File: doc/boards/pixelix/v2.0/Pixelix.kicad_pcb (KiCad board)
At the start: 2 copper layers, 101 x 50 mm, 32 parts, among them J1 Conn_01x02, J2 Conn_01x02, J3 Conn_01x03, J4 Conn_01x02, J5 Conn_02x05_Odd_Even, J6 Conn_01x02, J7 Conn_01x03, J8 Conn_01x02, Q1 NMOS_GSD_BSS138, Q2 PMOS_GDS_STD26P3LLH6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

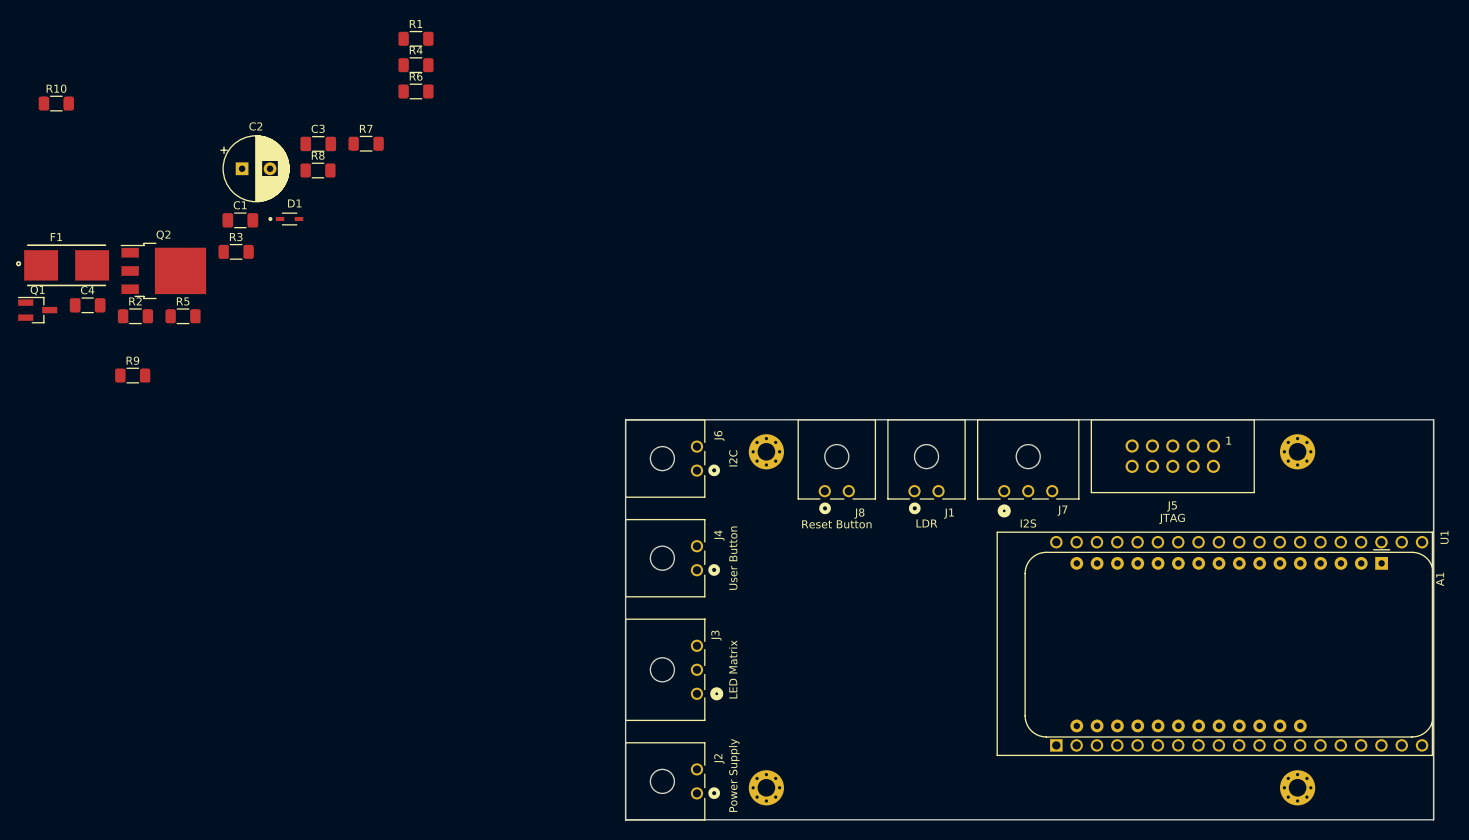
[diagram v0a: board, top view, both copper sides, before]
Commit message: Board v2.0 PCB - placed other components (R,C,FETs,...) - start routing
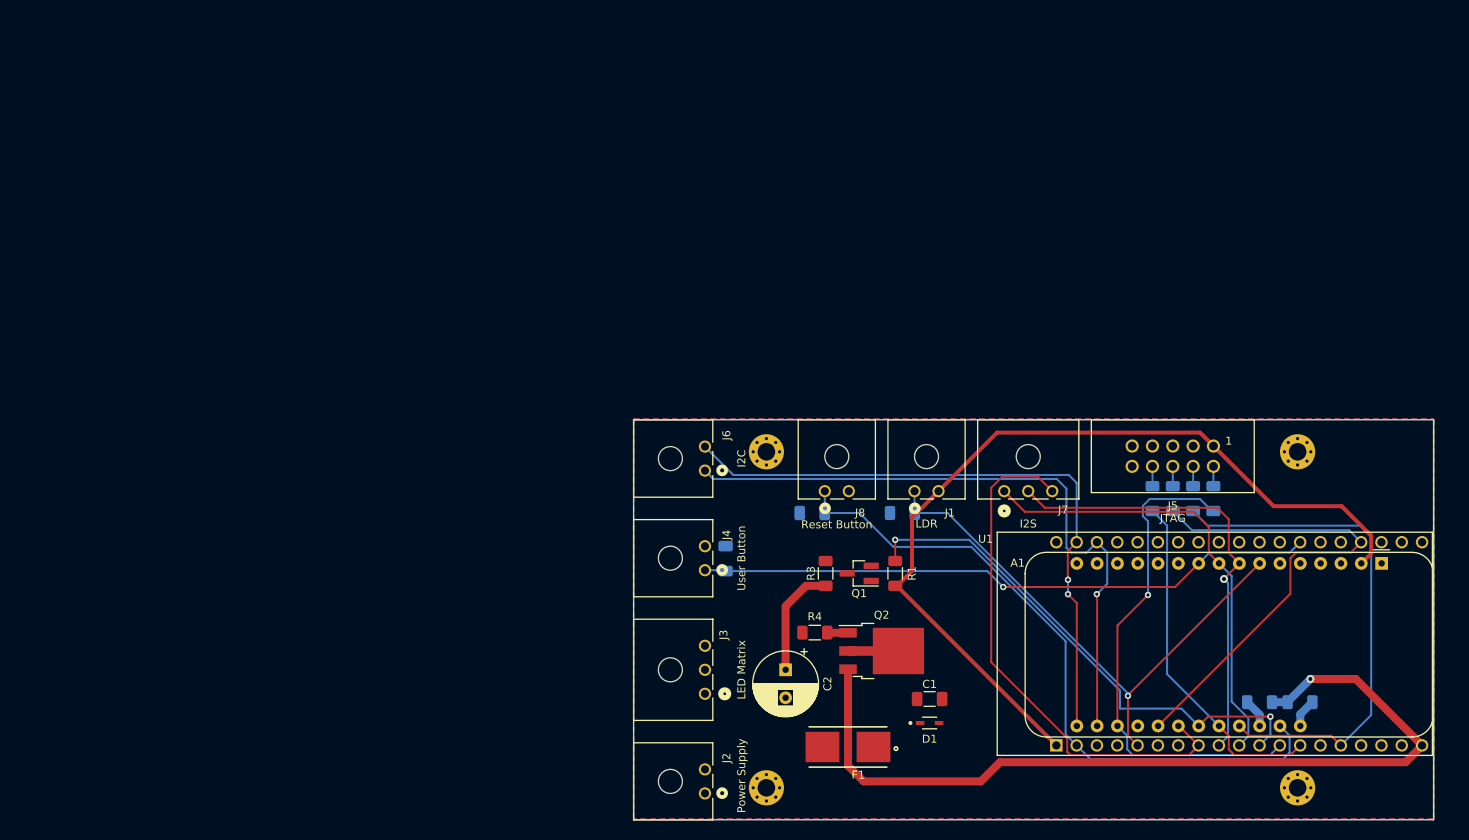
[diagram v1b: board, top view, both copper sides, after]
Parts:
- C3, C4, R10, R2, R5, R6, R7, R8, R9: moved to B.Cu
- moved R10 168.0 mm to (179.2, 105.4)
- moved R9 151.5 mm to (184.3, 105.4), turned to 180 degrees
- moved R5 130.8 mm to (173.5, 80.0), turned to -90 degrees
- moved F1 114.7 mm to (127.8, 111.0), turned to 180 degrees
- moved R8 112.1 mm to (165.9, 80.0), turned to -90 degrees
- moved R7 110.2 mm to (168.4, 80.0), turned to -90 degrees
- moved R6 109.7 mm to (170.9, 80.0), turned to -90 degrees
- moved Q1 107.8 mm to (129.2, 89.3), turned to 180 degrees
- moved C1 104.9 mm to (138.0, 105.0)
- moved D1 101.8 mm to (138.0, 108.0)
- moved Q2 101.5 mm to (132.0, 99.0)
- moved R2 99.0 mm to (134.6, 81.8), turned to 180 degrees
- moved C4 94.2 mm to (123.3, 81.8), turned to 180 degrees
- moved C2 92.4 mm to (120.0, 101.3), turned to -90 degrees
- moved R1 89.7 mm to (133.7, 89.3), turned to 90 degrees
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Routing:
- net /VCC-PROTECTED: track 0.00 -> 123.8 mm, vias 0 -> 1
- net +3V3: track 0.00 -> 109.7 mm
- net /RESET: track 0.00 -> 84.6 mm
- net /SCL: track 0.00 -> 82.2 mm, vias 0 -> 1
- net /SDA: track 0.00 -> 79.6 mm, vias 0 -> 2
- net /USER-BUTTON: track 0.00 -> 77.6 mm, vias 0 -> 1
- net /LDR-ANALOG-IN: track 0.00 -> 69.2 mm, vias 0 -> 1
- net /I2S_Data_IN: track 0.00 -> 66.5 mm
- net /LV-DATA-OUT: track 0.00 -> 65.2 mm, vias 0 -> 2
- net /MTCK: track 0.00 -> 65.0 mm
- net /MTDO: track 0.00 -> 62.6 mm
- net /MTMS: track 0.00 -> 62.4 mm, vias 0 -> 1
- net /I2S_CLK: track 0.00 -> 57.2 mm
- net /I2S_WS: track 0.00 -> 56.8 mm, vias 0 -> 1
- net /MTDI: track 0.00 -> 43.5 mm
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- added copper zone on B.Cu, net GND
- added copper zone on F.Cu, net GND
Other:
- board size 101 x 50 mm -> 100 x 50 mm

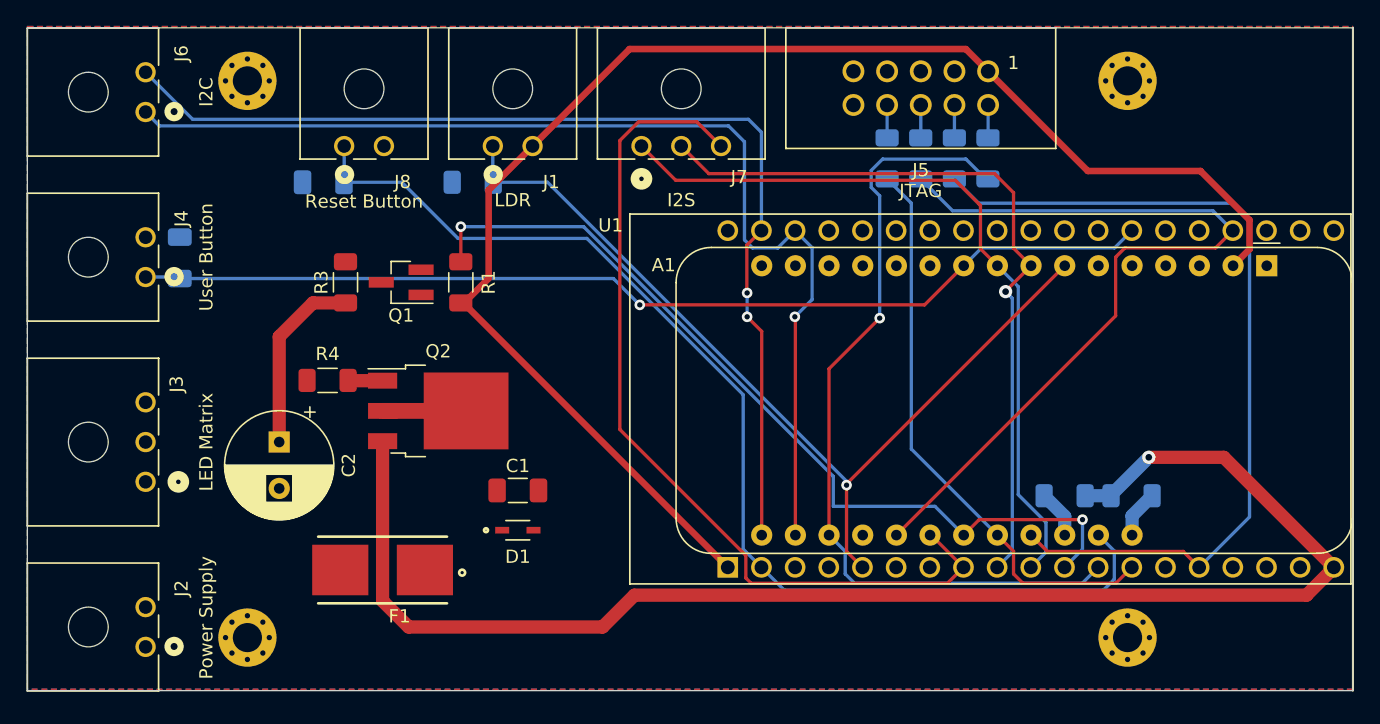
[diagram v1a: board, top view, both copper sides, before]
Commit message: Board v2.0 PCB - routing finished
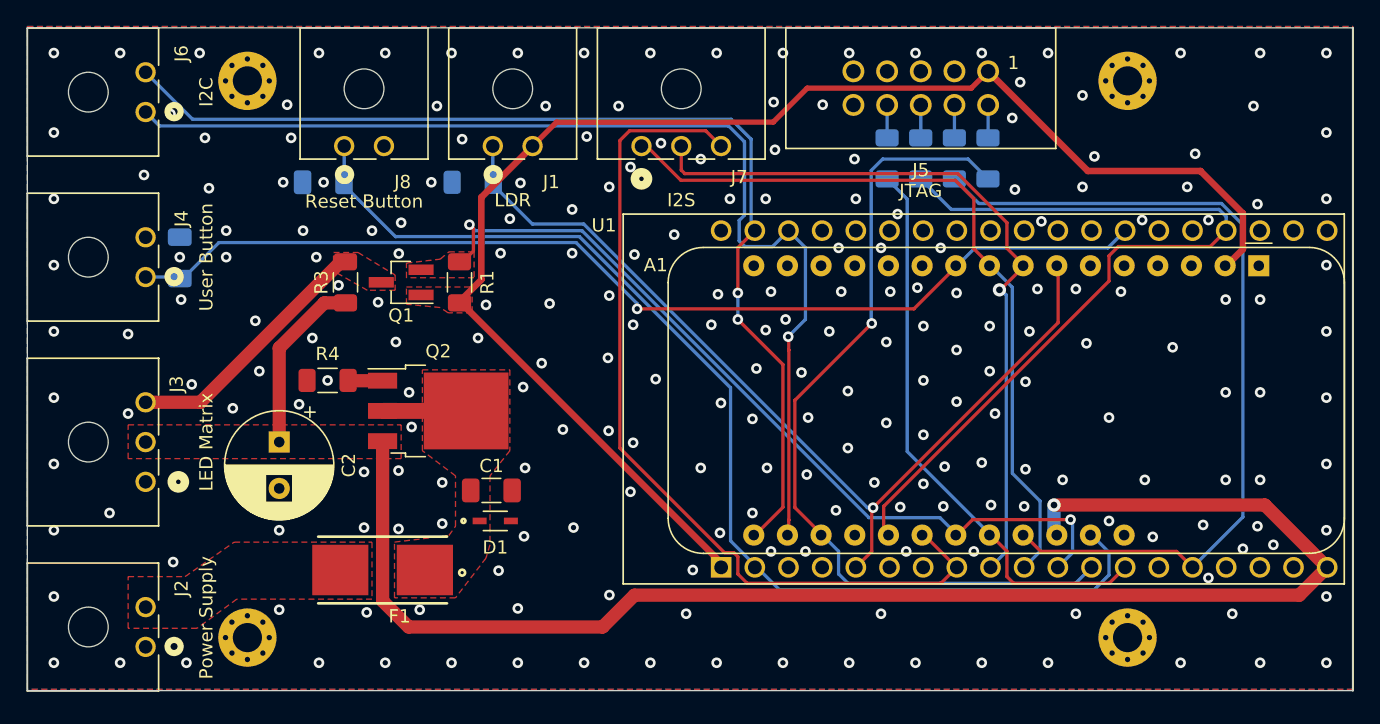
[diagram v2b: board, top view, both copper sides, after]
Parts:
- removed R10, R9: 0, Resistor_SMD:R_1206_3216Metric_Pad1.30x1.75mm_HandSolder
- moved C1 1.99 mm to (136.0, 105.0)
- moved D1 1.84 mm to (136.3, 107.3)
- moved A1 0.60 mm to (193.9, 88.0)
- moved U1 0.50 mm to (173.1, 98.1)
- moved R1 0.10 mm to (133.6, 89.3)
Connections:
- A1 pad 26: Net-(A1-Pad26) -> /VCC-PROTECTED
- A1 pad 28: Net-(A1-Pad28) -> unconnected-(A1-Pad28)
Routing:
- net /HV-DATA-OUT: track 0.00 -> 19.5 mm
- net Net-(A1-Pad26): track 3.61 -> 0.00 mm
- net Net-(A1-Pad28): track 3.59 -> 0.00 mm
- net +3V3: track 109.7 -> 107.0 mm
- net /USER-BUTTON: track 77.6 -> 79.8 mm
- net /LV-DATA-OUT: track 65.2 -> 63.1 mm
- net /LDR-ANALOG-IN: track 69.2 -> 70.8 mm
- net /MTMS: track 62.4 -> 63.9 mm
- net /SDA: track 79.6 -> 80.6 mm
- net /MTCK: track 65.0 -> 64.3 mm
- net /I2S_WS: track 56.8 -> 56.2 mm
- net /VCC-PROTECTED: track 123.8 -> 124.5 mm
- net /MTDO: track 62.6 -> 63.2 mm
- net GND: vias 0 -> 229
- added copper zone on F.Cu, net +3V3
- added copper zone on F.Cu, net /HV-DATA-OUT
- added copper zone on F.Cu, net /LV-DATA-OUT
- added copper zone on F.Cu, net /VCC-PROTECTED
- added copper zone on F.Cu, net Net-(C1-Pad1)
- added copper zone on F.Cu, net Net-(F1-Pad2)

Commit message: Board v2.0 PCB - small changes - create step file
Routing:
- net /MTMS: track 63.9 -> 65.2 mm
- net /RESET: track 84.1 -> 84.7 mm
- net GND: vias 229 -> 232

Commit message: Board v2.0 PCB - labeling PCB
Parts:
- added G***: LOGO, footprints:Pixelix_Logo_footprint, F.Cu at (186.3, 81.6)
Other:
- board text added: "${REVISION}"
- board text added: "BOT"
- board text added: "BlueAndi/esp-rgb-led-matrix"
- board text added: "Github Repository:"
- board text added: "TOP"

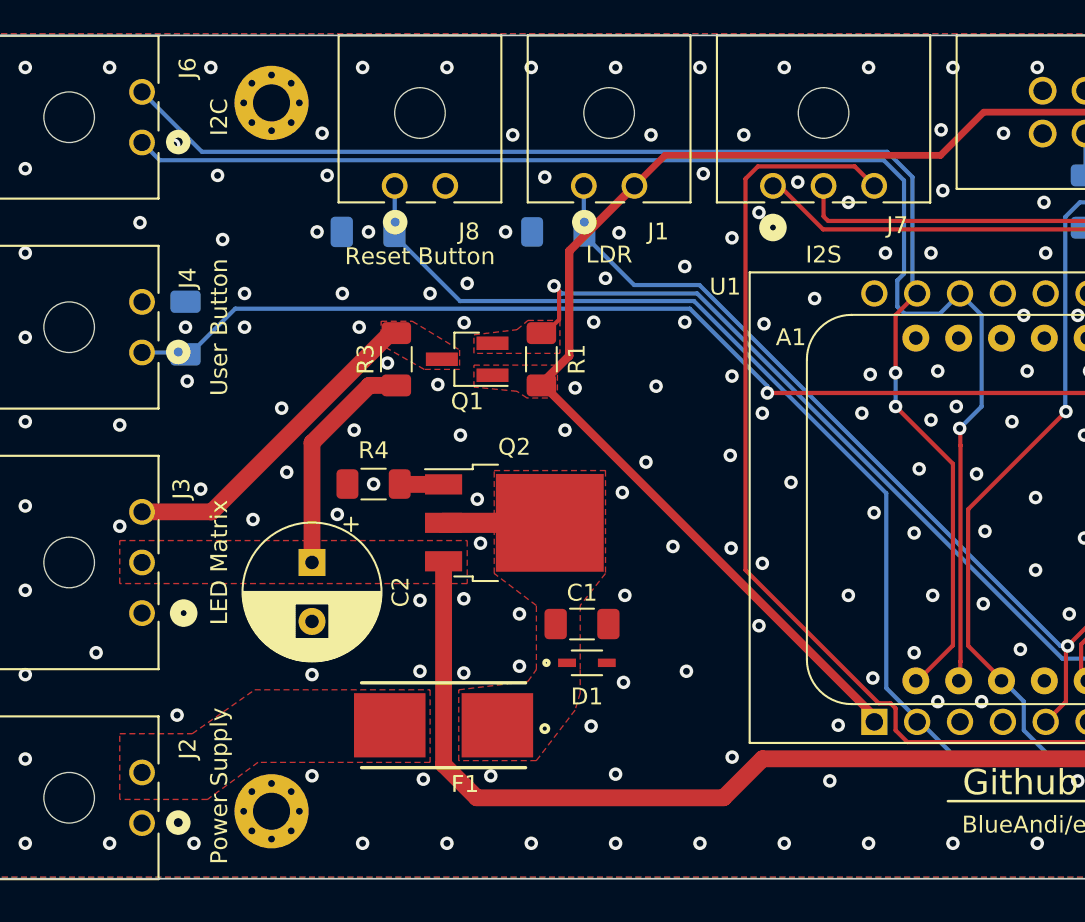
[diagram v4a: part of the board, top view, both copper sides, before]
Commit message: Board v2.0 PCB - rotate C2 (1000u Elko) - create new step file
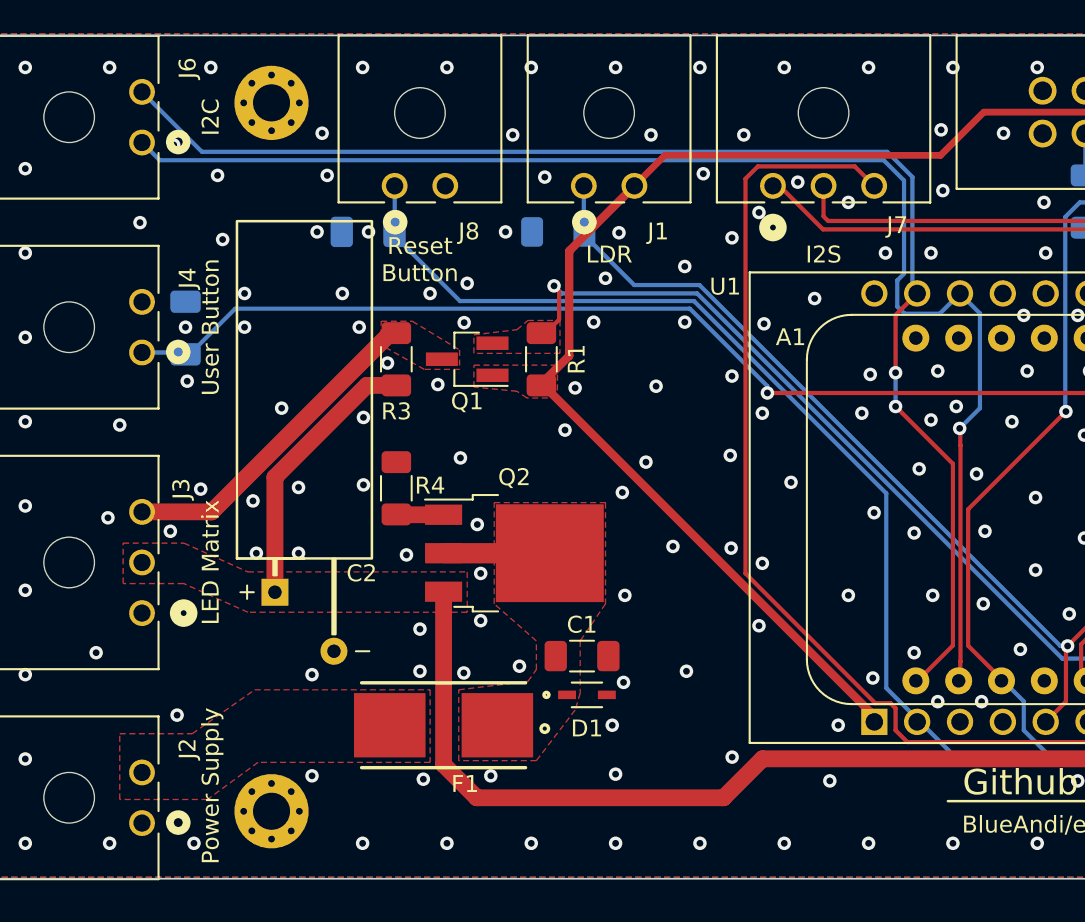
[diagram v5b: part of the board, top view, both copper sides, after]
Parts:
- C2: footprint Capacitor_THT:CP_Radial_D8.0mm_P3.50mm -> footprints:CP_Radial_D8.0mm_P3.50mm_horizontal
- moved C2 2.21 mm to (117.8, 101.1), turned to 0 degrees
- moved C1 1.90 mm to (136.0, 106.9)
- moved D1 1.90 mm to (136.3, 109.2)
- moved Q2 1.80 mm to (132.0, 100.8)
- moved R4 1.37 mm to (125.0, 97.0), turned to 90 degrees
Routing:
- net /VCC-PROTECTED: track 124.5 -> 125.4 mm
- net GND: vias 232 -> 234
